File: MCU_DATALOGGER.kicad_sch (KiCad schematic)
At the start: 1 part

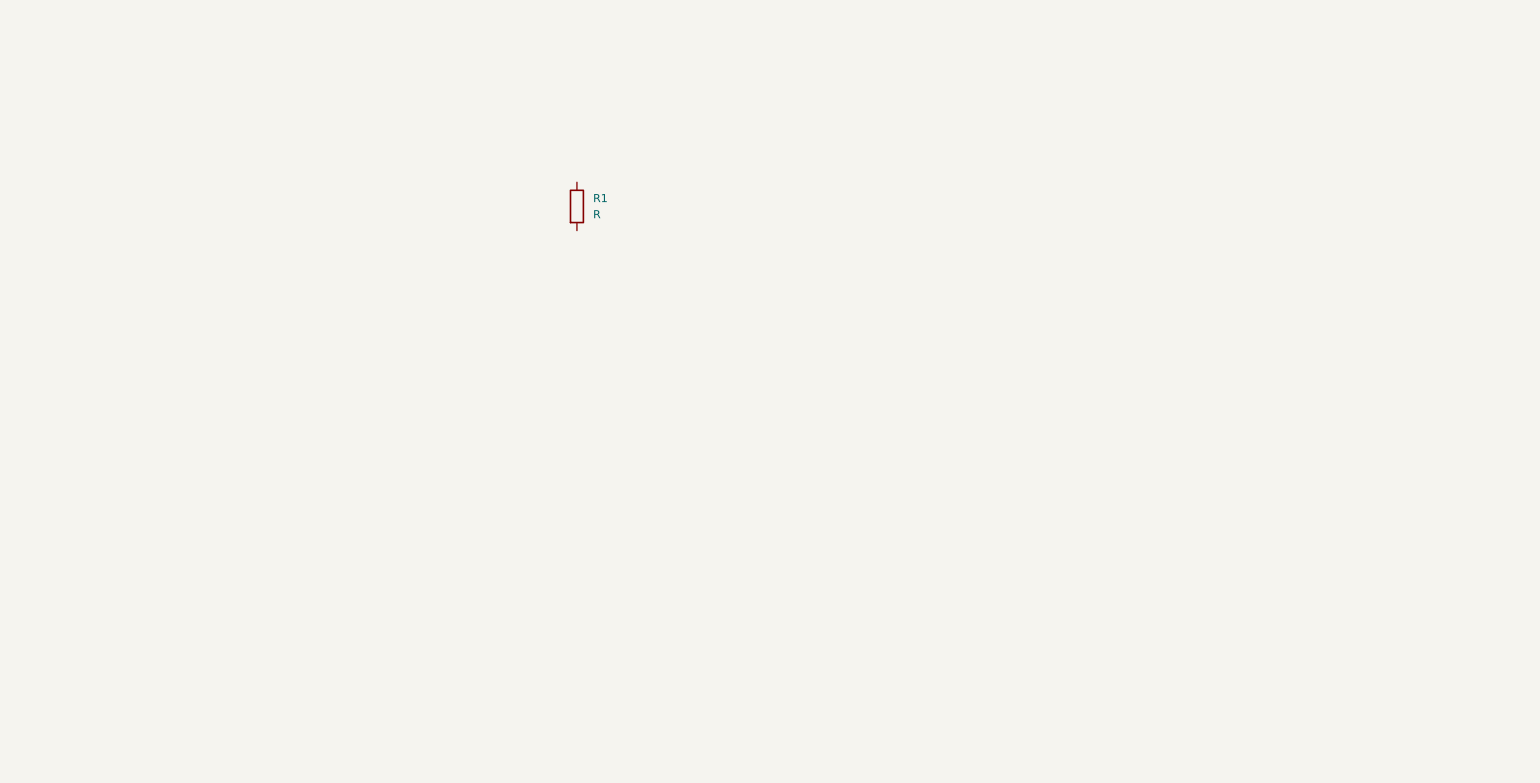
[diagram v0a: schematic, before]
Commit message: Added all symbols to the schematics
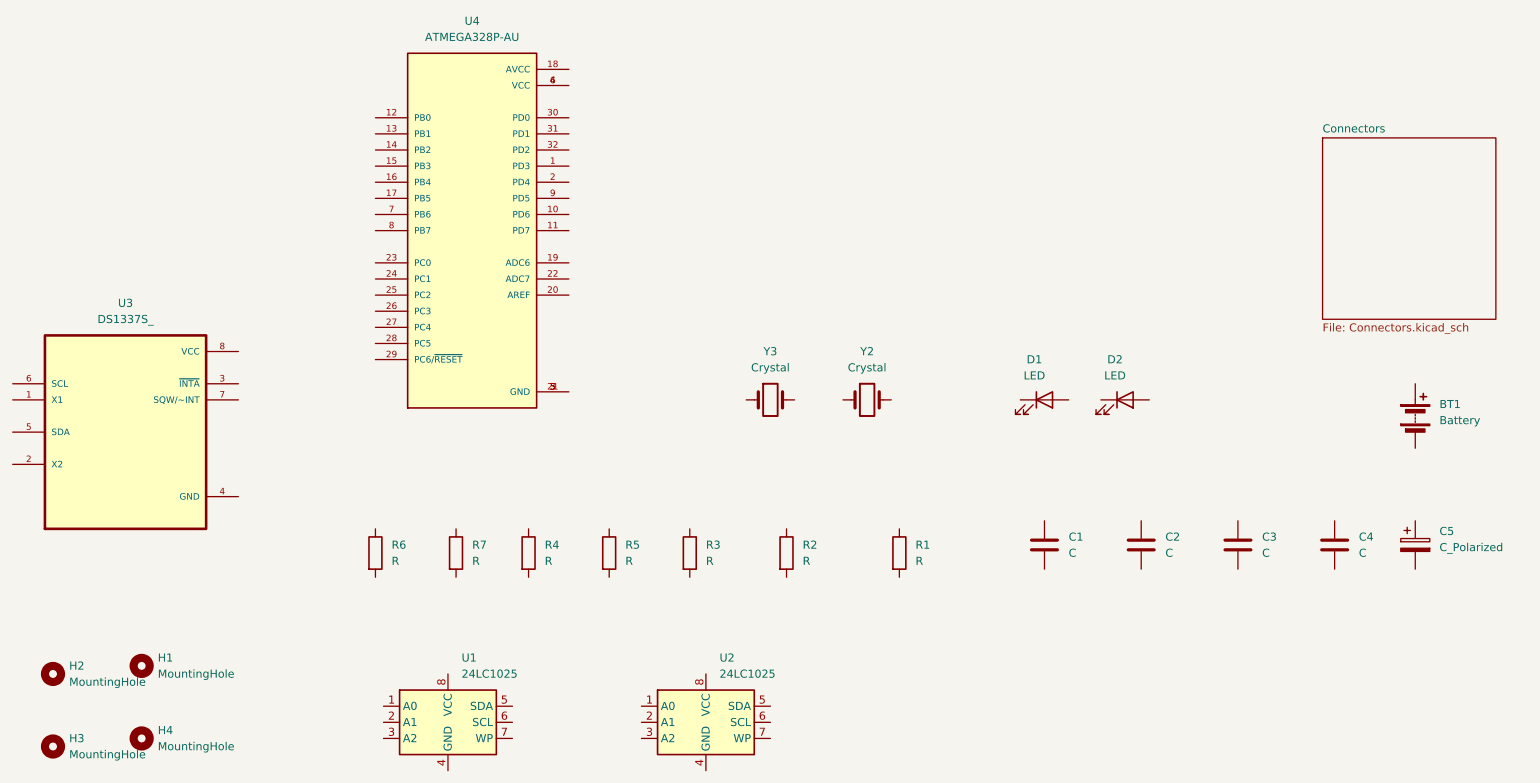
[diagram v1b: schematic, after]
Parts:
- added BT1: Battery, symbol Device:Battery
- added C1, C2, C3, C4: C, symbol Device:C
- added C5: C_Polarized, symbol Device:C_Polarized
- added D1, D2: LED, symbol Device:LED
- added H1, H2, H3, H4: MountingHole, symbol Mechanical:MountingHole
- added R2, R3, R4, R5, R6, R7: R, symbol Device:R
- added U1, U2: 24LC1025, symbol Memory_EEPROM:24LC1025
- added U3: DS1337S_, DS1337S_:SOIC127P600X175-8N, symbol DS1337S_:DS1337S_
- added U4: ATMEGA328P-AU, ATMEGA328P-AU:QFP80P900X900X120-32N, symbol ATMEGA328P-AU:ATMEGA328P-AU
- added Y2, Y3: Crystal, symbol Device:Crystal
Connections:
- new net: U4.21 (GND), U4.3 (GND), U4.5 (GND)
- new net: U4.4 (VCC), U4.6 (VCC)
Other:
- added sheet Connectors (Connectors.kicad_sch)
- moved on the sheet: R1
